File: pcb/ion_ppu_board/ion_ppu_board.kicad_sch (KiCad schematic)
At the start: 12 parts, among them Q1 IRFH5250, Q2 Q_PMOS_GSD

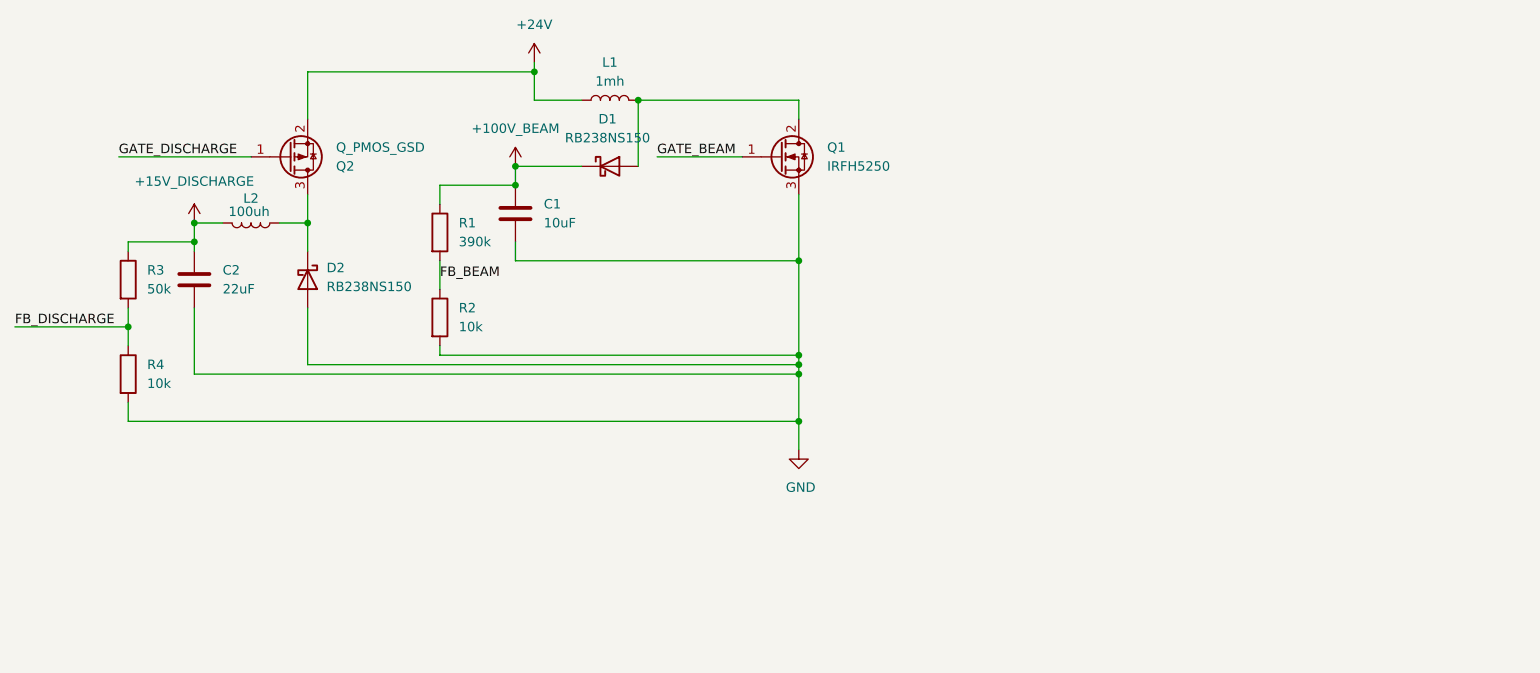
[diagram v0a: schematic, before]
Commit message: Day 10: Complete MCU mapping and clean up schematic ERC
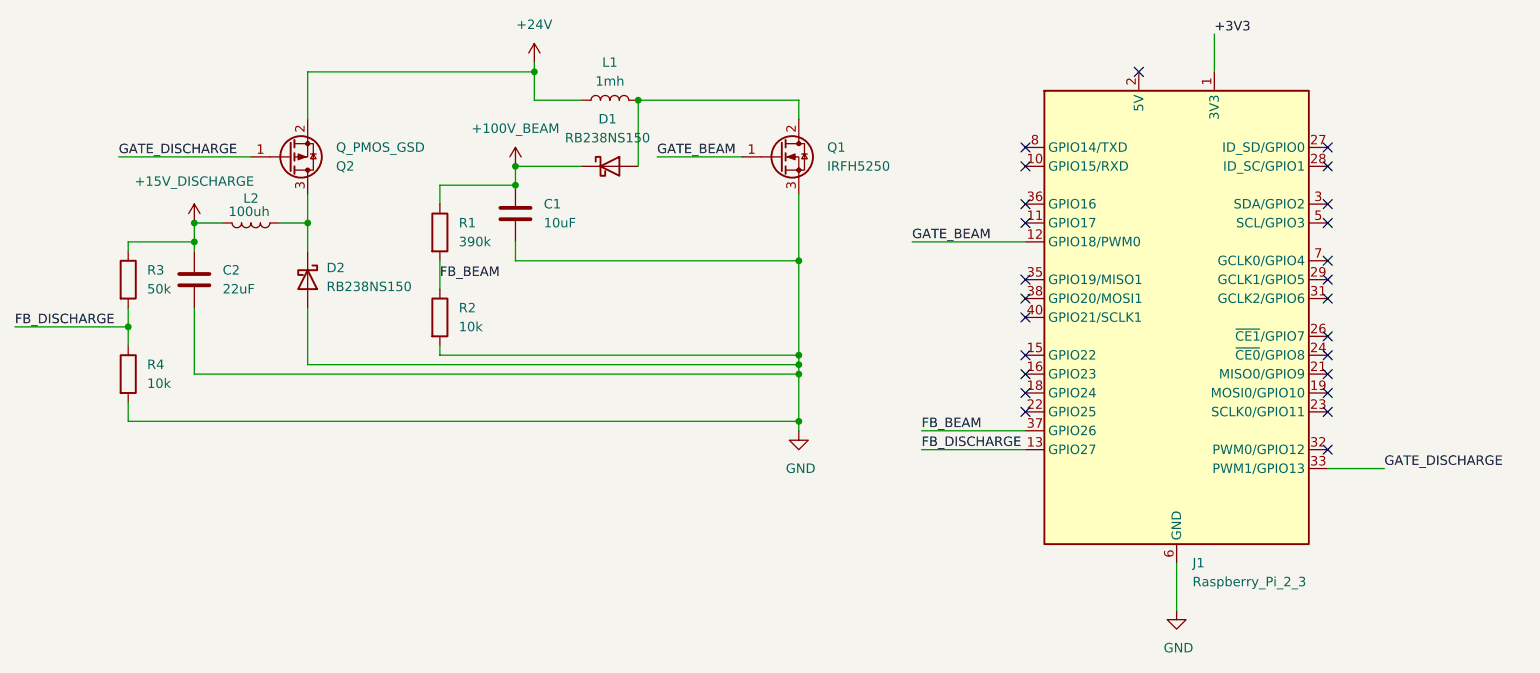
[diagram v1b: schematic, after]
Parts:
- added J1: Raspberry_Pi_2_3, symbol Connector:Raspberry_Pi_2_3
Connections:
- net FB_BEAM: now also J1.37 (GPIO26)
- net FB_DISCHARGE: now also J1.13 (GPIO27)
- net GATE_BEAM: now also J1.12 (GPIO18/PWM0)
- net GATE_DISCHARGE: now also J1.33 (PWM1/GPIO13)
- net GND: now also J1.14 (GND), J1.20 (GND), J1.25 (GND), J1.30 (GND), J1.34 (GND), J1.39 (GND), J1.6 (GND), J1.9 (GND)
- new net: J1.2 (5V), J1.4 (5V)
- new net +3V3: J1.1 (3V3), J1.17 (3V3)
- no-connect marks 0 -> 25

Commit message: Complete all component footprint assignments in KiCad
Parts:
- C1, C2: footprint (none) -> Capacitor_SMD:C_0805_2012Metric
- D1, D2, Q1, Q2: footprint (none) -> Package_TO_SOT_SMD:TO-252-2
- J1: footprint (none) -> Connector_PinHeader_2.54mm:PinHeader_2x20_P2.54mm_Vertical
- L1, L2: footprint (none) -> Inductor_SMD:L_12x12mm_H8mm
- R1, R2, R3, R4: footprint (none) -> Resistor_SMD:R_0805_2012Metric
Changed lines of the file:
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@@
 			)
 		)
-		(property "Footprint" ""
+		(property "Footprint" "Capacitor_SMD:C_0805_2012Metric"
 			(at 96.2152 85.09 0)
 			(hide yes)
@@
 			)
 		)
-		(property "Footprint" ""
+		(property "Footprint" "Inductor_SMD:L_12x12mm_H8mm"
 			(at 59.69 82.55 0)
 			(hide yes)
@@
 			)
 		)
-		(property "Footprint" ""
+		(property "Footprint" "Resistor_SMD:R_0805_2012Metric"
 			(at 41.402 90.17 90)
 			(hide yes)
@@
 			)
 		)
-		(property "Footprint" ""
+		(property "Footprint" "Package_TO_SOT_SMD:TO-252-2"
 			(at 107.95 74.93 0)
 			(hide yes)
@@
 			)
 		)
-		(property "Footprint" ""
+		(property "Footprint" "Resistor_SMD:R_0805_2012Metric"
 			(at 41.402 102.87 90)
 			(hide yes)
@@
 			)
 		)
-		(property "Footprint" ""
+		(property "Footprint" "Connector_PinHeader_2.54mm:PinHeader_2x20_P2.54mm_Vertical"
 			(at 184.15 95.25 0)
 			(hide yes)
@@
 			)
 		)
-		(property "Footprint" ""
+		(property "Footprint" "Package_TO_SOT_SMD:TO-252-2"
 			(at 67.31 90.17 0)
 			(hide yes)
@@
 			)
 		)
-		(property "Footprint" ""
+		(property "Footprint" "Capacitor_SMD:C_0805_2012Metric"
 			(at 53.0352 93.98 0)
 			(hide yes)
@@
 			)
 		)
-		(property "Footprint" ""
+		(property "Footprint" "Package_TO_SOT_SMD:TO-252-2"
 			(at 69.85 76.2 0)
 			(hide yes)
@@
 			)
 		)
-		(property "Footprint" ""
+		(property "Footprint" "Resistor_SMD:R_0805_2012Metric"
 			(at 83.312 95.25 90)
 			(hide yes)
@@
 			)
 		)
-		(property "Footprint" ""
+		(property "Footprint" "Package_TO_SOT_SMD:TO-252-2"
 			(at 135.89 71.12 0)
 			(hide yes)
@@
 			)
 		)
-		(property "Footprint" ""
+		(property "Footprint" "Inductor_SMD:L_12x12mm_H8mm"
 			(at 107.95 66.04 0)
 			(hide yes)
@@
 			)
 		)
-		(property "Footprint" ""
+		(property "Footprint" "Resistor_SMD:R_0805_2012Metric"
 			(at 83.312 83.82 90)
 			(hide yes)
